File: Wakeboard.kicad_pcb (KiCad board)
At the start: 2 copper layers, 30.6 x 58.6 mm, 34 parts, among them CN1 JST S2B-PH-SM4-TB(LF)(SN), J2 HCTL HC-TYPE-C-16P-01A, Q1 DMP2045UQ-7, SW1 TS-1088-AR02016, SW2 TS-1088-AR02016, U1 RT9080-33GJ5, U2 ESP32-S3-MINI-1, U3 LIS3DHTR_C15134, U4 MCP73831T-2ACI/OT

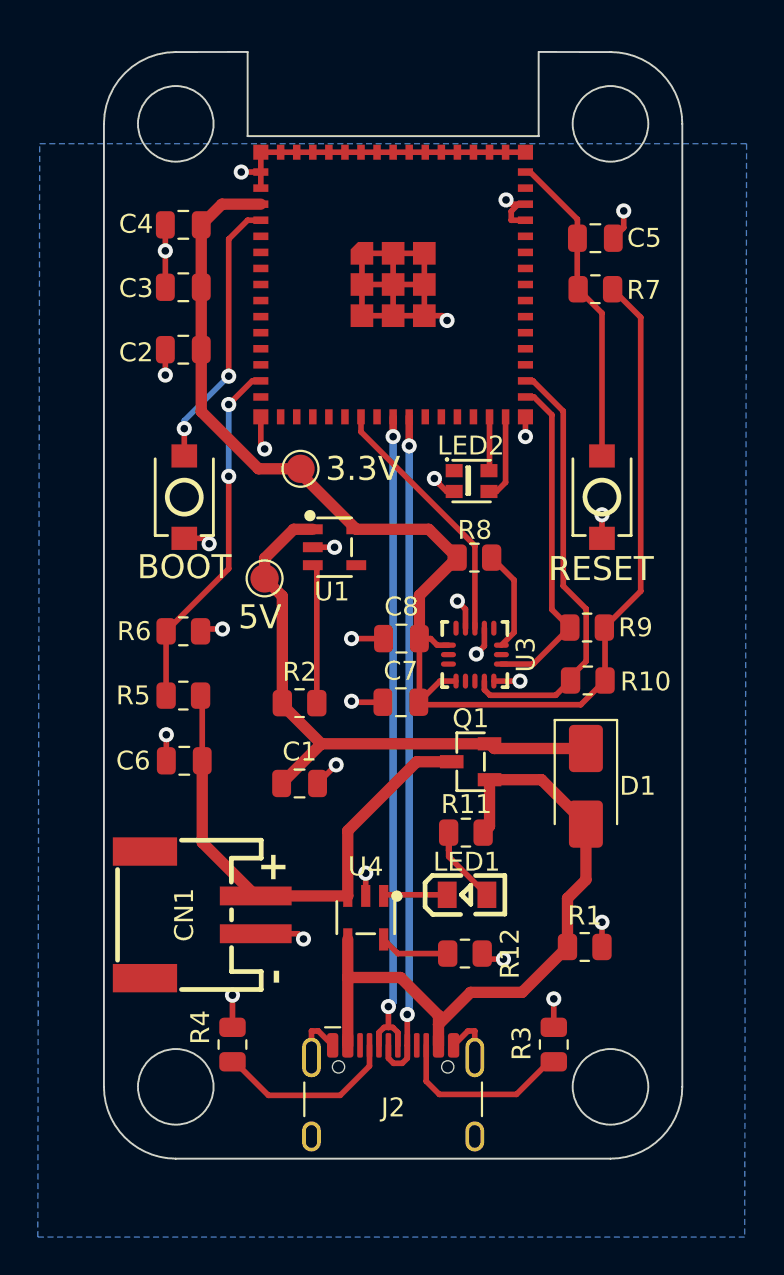
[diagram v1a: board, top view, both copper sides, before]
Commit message: Shift battery socket
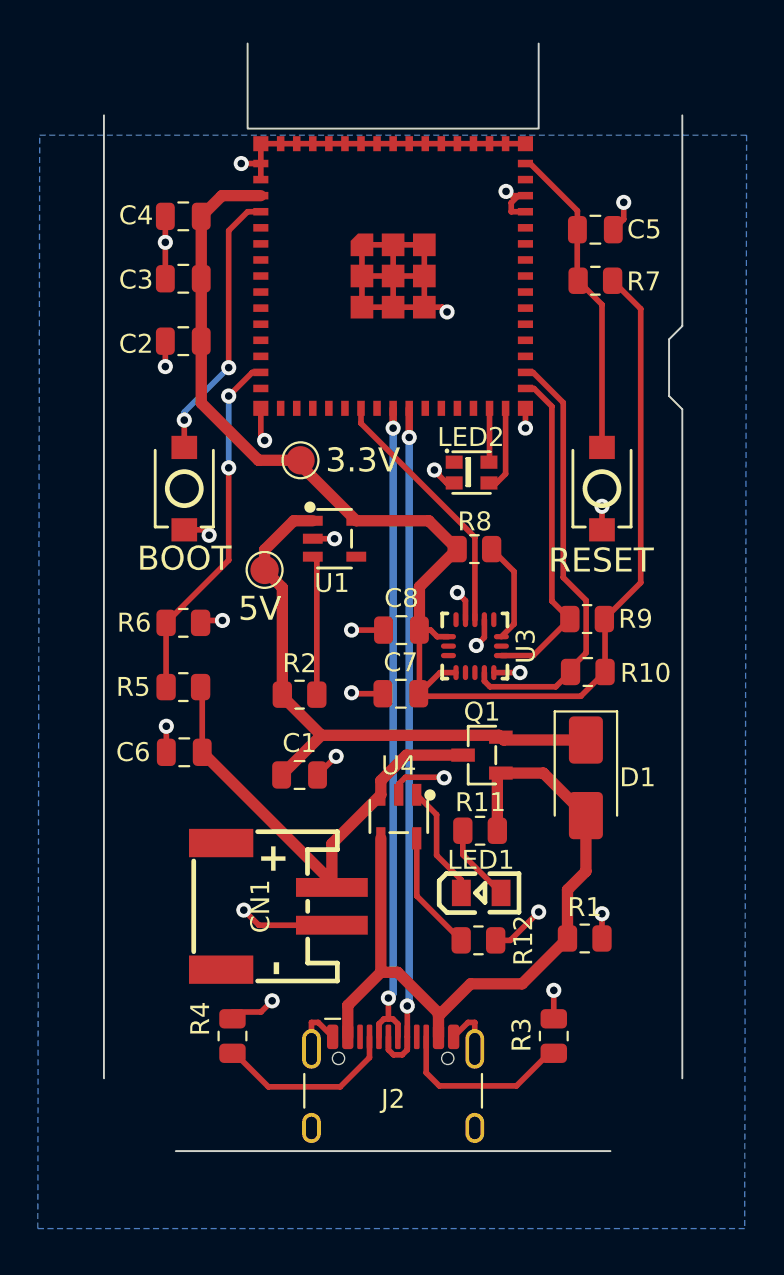
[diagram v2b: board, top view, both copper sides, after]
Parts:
- moved U4 5.63 mm to (127.8, 84.9)
- moved CN1 4.06 mm to (121.3, 89.7)
- moved R12 1.00 mm to (132.0, 91.5)
- moved LED1 0.76 mm to (132.2, 88.9)
- moved R11 0.76 mm to (132.1, 85.7)
- moved Q1 0.69 mm to (132.2, 81.7)
- moved C1 0.45 mm to (122.5, 82.7)
- moved C2 0.45 mm to (116.4, 59.7)
- moved C3 0.45 mm to (116.4, 56.4)
- moved C4 0.45 mm to (116.4, 53.1)
- moved C6 0.45 mm to (116.5, 81.5)
- moved C7 0.45 mm to (127.9, 78.4)
- moved C8 0.45 mm to (127.9, 75.0)
- moved D1 0.45 mm to (137.7, 82.8)
- moved J2 0.45 mm to (127.5, 100.3)
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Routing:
- net GND: track 82.0 -> 88.9 mm
- net VBUS: track 37.3 -> 40.4 mm
- net Net-(LED1--): track 3.38 -> 6.17 mm
- net Net-(U4-PROG): track 3.70 -> 6.37 mm
- net VBAT: track 27.1 -> 25.1 mm
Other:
- outline, holes or cut-outs redrawn

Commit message: Remove mounting holes. Fix minor things
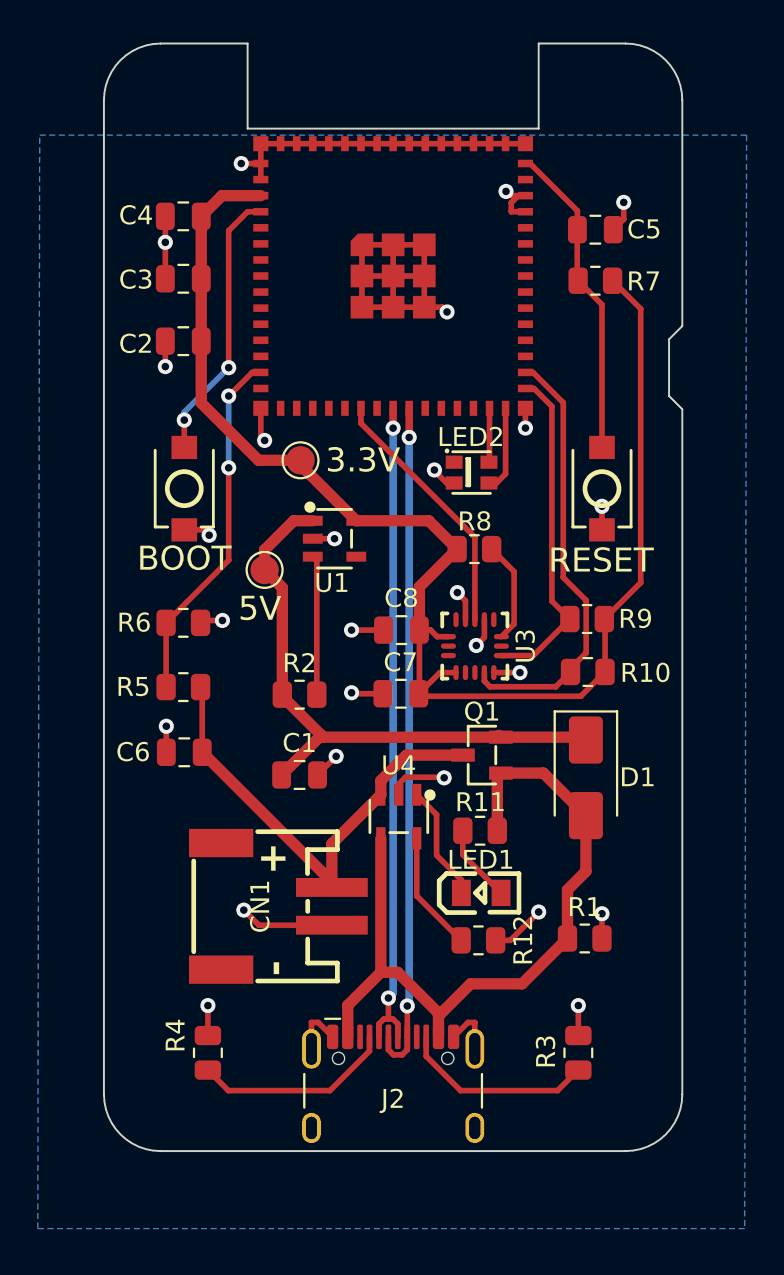
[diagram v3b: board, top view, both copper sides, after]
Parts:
- moved R3 1.57 mm to (137.3, 97.4)
- moved R4 1.57 mm to (117.7, 97.4)
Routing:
- net Net-(J2-CC1): track 9.77 -> 10.6 mm
- net Net-(J2-CC2): track 9.58 -> 10.3 mm
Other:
- outline, holes or cut-outs redrawn
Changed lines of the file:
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@@
 	(footprint "Resistor_SMD:R_0805_2012Metric"
 		(layer "F.Cu")
-		(at 136 96.5125 -90)
+		(at 137.3 97.4 -90)
 		(descr "Resistor SMD 0805 (2012 Metric), square (rectangular) end terminal, IPC_7351 nominal, (Body size source: IPC-SM-782 page 72, https://www.pcb-3d.com/wordpress/wp-content/uploads/ipc-sm-782a_amendment_1_and_2.pdf), generated with kicad-footprint-generator")
 		(tags "resistor")
@@
 	(footprint "Resistor_SMD:R_0805_2012Metric"
 		(layer "F.Cu")
-		(at 119 96.5125 -90)
+		(at 117.7 97.4 -90)
 		(descr "Resistor SMD 0805 (2012 Metric), square (rectangular) end terminal, IPC_7351 nominal, (Body size source: IPC-SM-782 page 72, https://www.pcb-3d.com/wordpress/wp-content/uploads/ipc-sm-782a_amendment_1_and_2.pdf), generated with kicad-footprint-generator")
 		(tags "resistor")
@@
 		(layer "B.SilkS")
 	)
+	(gr_arc
+		(start 142.8 99.6)
+		(mid 141.92132 101.72132)
+		(end 139.8 102.6)
+		(stroke
+			(width 0.1)
+			(type default)
+		)
+		(layer "Edge.Cuts")
+	)
 	(gr_line
 		(start 142.1 59.65)
@@
 	)
 	(gr_line
-		(start 142.799658 47.803044)
+		(start 142.8 47)
 		(end 142.8 58.95)
 		(stroke
@@
 	(gr_line
 		(start 142.8 63.35)
-		(end 142.8 98.75)
+		(end 142.8 99.6)
 		(stroke
 			(width 0.1)
@@
 	)
 	(gr_line
-		(start 119.8 48.45)
+		(start 119.8 48.5)
 		(end 119.8 44)
 		(stroke
@@
 		(layer "Edge.Cuts")
 	)
+	(gr_arc
+		(start 115.2 102.6)
+		(mid 113.07868 101.72132)
+		(end 112.2 99.6)
+		(stroke
+			(width 0.1)
+			(type default)
+		)
+		(layer "Edge.Cuts")
+	)
+	(gr_arc
+		(start 139.8 44)
+		(mid 141.92132 44.87868)
+		(end 142.8 47)
+		(stroke
+			(width 0.1)
+			(type default)
+		)
+		(layer "Edge.Cuts")
+	)
 	(gr_line
-		(start 112.199829 47.797938)
-		(end 112.2 98.75)
+		(start 112.2 47)
+		(end 112.2 99.6)
 		(stroke
 			(width 0.1)
@@
 	)
 	(gr_line
-		(start 116 102.6)
-		(end 139 102.6)
+		(start 115.2 102.6)
+		(end 139.8 102.6)
 		(stroke
 			(width 0.1)
@@
 	(gr_line
 		(start 135.2 44)
-		(end 135.2 48.45)
+		(end 139.8 44)
+		(stroke
+			(width 0.1)
+			(type default)
+		)
+		(layer "Edge.Cuts")
+	)
+	(gr_line
+		(start 119.8 44)
+		(end 115.2 44)
+		(stroke
+			(width 0.1)
+			(type default)
+		)
+		(layer "Edge.Cuts")
+	)
+	(gr_line
+		(start 135.2 44)
+		(end 135.2 48.5)
 		(stroke
 			(width 0.1)
@@
 		(layer "Edge.Cuts")
 	)
+	(gr_arc
+		(start 112.2 47)
+		(mid 113.07868 44.87868)
+		(end 115.2 44)
+		(stroke
+			(width 0.1)
+			(type default)
+		)
+		(layer "Edge.Cuts")
+	)
 	(gr_text "-"
 		(at 122.1 93.35 90)
@@
 	)
 	(segment
-		(start 133.35 80.85)
-		(end 133.2 80.7)
+		(start 120.7 71.85)
+		(end 120.7 70.78934)
 		(width 0.6)
 		(layer "F.Cu")
@@
 	)
 	(segment
-		(start 120.7 71.85)
-		(end 120.7 70.78934)
+		(start 133.2 80.7)
+		(end 133.1 80.6)
 		(width 0.6)
 		(layer "F.Cu")
@@
 	)
 	(segment
-		(start 133.2 80.7)
-		(end 133.1 80.6)
+		(start 137.55 80.7)
+		(end 137.7 80.85)
 		(width 0.6)
 		(layer "F.Cu")
@@
 	)
 	(segment
-		(start 122.23934 69.25)
-		(end 123.25 69.25)
+		(start 133.2 80.7)
+		(end 123.8 80.7)
 		(width 0.6)
 		(layer "F.Cu")
@@
 	)
 	(segment
-		(start 133.1 80.6)
-		(end 123.7 80.6)
+		(start 122.23934 69.25)
+		(end 123.25 69.25)
 		(width 0.6)
 		(layer "F.Cu")
@@
 	)
 	(segment
+		(start 123.8 80.7)
+		(end 123.7 80.6)
+		(width 0.6)
+		(layer "F.Cu")
+		(net 31)
+	)
+	(segment
+		(start 133.2 80.7)
+		(end 137.55 80.7)
+		(width 0.6)
+		(layer "F.Cu")
+		(net 31)
+	)
+	(segment
 		(start 121.6375 78.45)
 		(end 121.6375 78.5375)
@@
 	)
 	(segment
-		(start 137.7 80.85)
-		(end 133.35 80.85)
-		(width 0.6)
-		(layer "F.Cu")
-		(net 31)
-	)
-	(segment
 		(start 121.6375 78.45)
 		(end 121.6375 72.7875)
@@
 	)
 	(segment
-		(start 121.1 94.65)
-		(end 120.5094 95.2406)
+		(start 117.7 96.4875)
+		(end 117.7 94.9)
 		(width 0.3)
 		(layer "F.Cu")
@@
 	)
 	(segment
-		(start 120.5094 95.2406)
-		(end 119 95.2406)
-		(width 0.3)
-		(layer "F.Cu")
-		(net 32)
-	)
-	(segment
 		(start 134.5 52.9)
 		(end 133.7483 52.9)
@@
 	)
 	(segment
+		(start 137.3 96.4875)
+		(end 137.3 94.9)
+		(width 0.3)
+		(layer "F.Cu")
+		(net 32)
+	)
+	(segment
 		(start 127.5 56.3)
 		(end 127.5 57.95)
@@
 	)
 	(segment
-		(start 136 94.09475)
-		(end 136 95.40525)
-		(width 0.3)
-		(layer "F.Cu")
-		(net 32)
-	)
-	(segment
 		(start 128.35 49.3)
 		(end 127.5 49.3)
@@
 	)
 	(via
-		(at 138.55 68.4835)
+		(at 117.7 94.9)
 		(size 0.8)
 		(drill 0.4)
@@
 	)
 	(via
-		(at 115.5 80.1225)
+		(at 138.55 68.4835)
 		(size 0.8)
 		(drill 0.4)
@@
 	)
 	(via
-		(at 124.4 70.2)
+		(at 115.5 80.1225)
 		(size 0.8)
 		(drill 0.4)
@@
 	)
 	(via
-		(at 134.210794 77.282498)
+		(at 124.4 70.2)
 		(size 0.8)
 		(drill 0.4)
@@
 	)
 	(via
-		(at 134.5 64.3465)
+		(at 134.210794 77.282498)
 		(size 0.8)
 		(drill 0.4)
@@
 	)
 	(via
-		(at 135.2 89.95)
+		(at 134.5 64.3465)
 		(size 0.8)
 		(drill 0.4)
@@
 	)
 	(via
-		(at 121.1 94.65)
+		(at 135.2 89.95)
 		(size 0.8)
 		(drill 0.4)
@@
 	)
 	(via
-		(at 136 94.09475)
+		(at 130.2 82.85)
 		(size 0.8)
 		(drill 0.4)
@@
 	)
 	(via
-		(at 130.2 82.85)
+		(at 139.7 52.4056)
 		(size 0.8)
 		(drill 0.4)
@@
 	)
 	(via
-		(at 139.7 52.4056)
+		(at 129.683228 66.562164)
 		(size 0.8)
 		(drill 0.4)
@@
 	)
 	(via
-		(at 129.683228 66.562164)
+		(at 115.448 54.5198)
 		(size 0.8)
 		(drill 0.4)
@@
 	)
 	(via
-		(at 115.448 54.5198)
+		(at 137.3 94.9)
 		(size 0.8)
 		(drill 0.4)
@@
 	)
 	(segment
-		(start 134.025 99.15)
-		(end 129.945 99.15)
+		(start 137.0175 98.595)
+		(end 137.005 98.595)
+		(width 0.3)
+		(layer "F.Cu")
+		(net 38)
+	)
+	(segment
+		(start 137.3 98.3125)
+		(end 137.0175 98.595)
 		(width 0.3)
 		(layer "F.Cu")
@@
 	)
 	(segment
-		(start 129.25 98.455)
+		(start 129.25 97.580305)
 		(end 129.25 96.555)
 		(width 0.3)
@@
 	)
 	(segment
-		(start 135.875 97.3)
-		(end 134.025 99.15)
+		(start 131.069695 99.4)
+		(end 129.25 97.580305)
 		(width 0.3)
 		(layer "F.Cu")
@@
 	)
 	(segment
-		(start 129.945 99.15)
-		(end 129.25 98.455)
+		(start 136.2 99.4)
+		(end 131.069695 99.4)
 		(width 0.3)
 		(layer "F.Cu")
@@
 	)
 	(segment
-		(start 120.9 99.2)
-		(end 124.7 99.2)
+		(start 137.005 98.595)
+		(end 136.2 99.4)
+		(width 0.3)
+		(layer "F.Cu")
+		(net 38)
+	)
+	(segment
+		(start 126.25 97.30812)
+		(end 126.25 96.555)
 		(width 0.3)
 		(layer "F.Cu")
@@
 	)
 	(segment
-		(start 119 97.3)
-		(end 120.9 99.2)
+		(start 117.7 98.3125)
+		(end 118.7875 99.4)
 		(width 0.3)
 		(layer "F.Cu")
@@
 	)
 	(segment
-		(start 124.7 99.2)
-		(end 126.25 97.65)
+		(start 124.15812 99.4)
+		(end 126.25 97.30812)
 		(width 0.3)
 		(layer "F.Cu")
@@
 	)
 	(segment
-		(start 126.25 97.65)
-		(end 126.25 96.555)
+		(start 118.7875 99.4)
+		(end 124.15812 99.4)
 		(width 0.3)
 		(layer "F.Cu")

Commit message: Enclosure OpenSCAD files
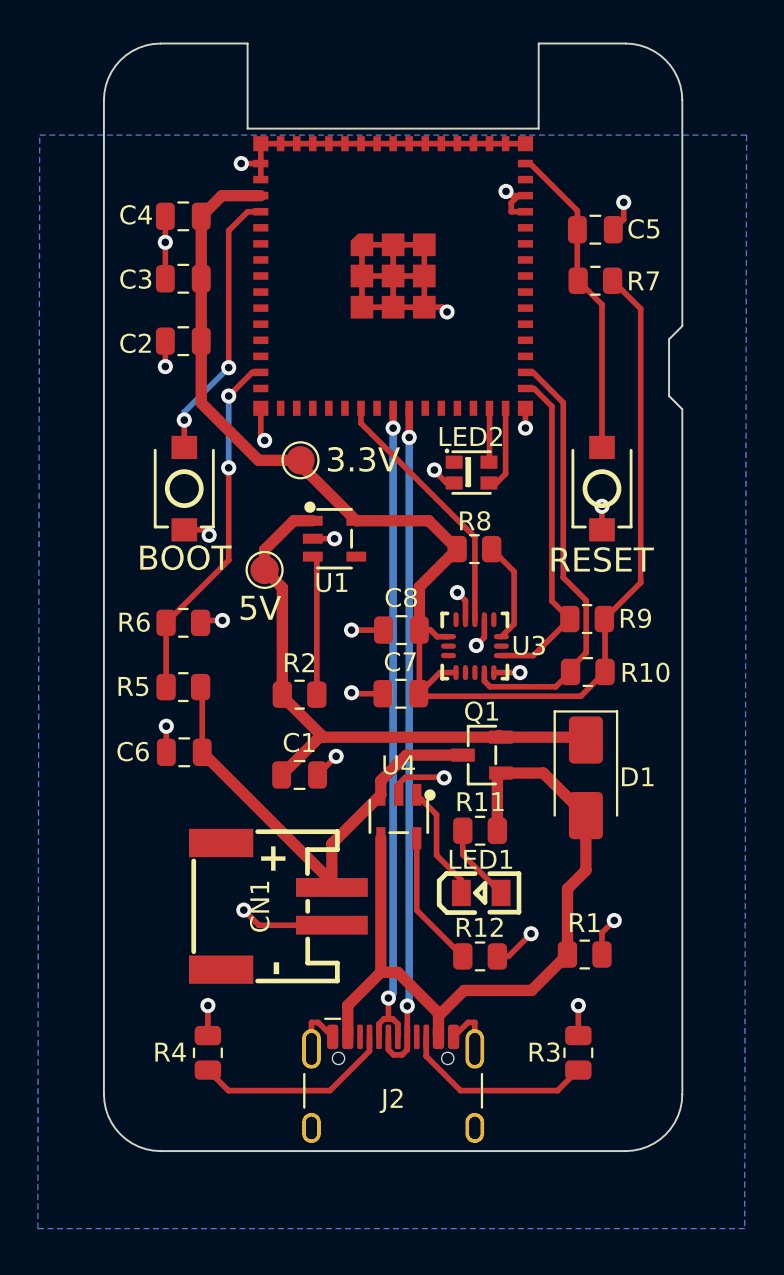
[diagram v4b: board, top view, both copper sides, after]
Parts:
- moved R12 0.85 mm to (132.1, 92.3)
- moved R1 0.85 mm to (137.6, 92.2)
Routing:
- net Net-(U4-PROG): track 6.37 -> 7.26 mm
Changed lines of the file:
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@@
 		(tags "resistor")
 		(property "Reference" "R3"
-			(at -0.0625 1.7 90)
+			(at 0 1.8 180)
 			(layer "F.SilkS")
 			(effects
@@
 		)
 		(property "Value" "5.1K"
-			(at 0.0375 -0.1 90)
+			(at 0 -1.8 90)
 			(layer "F.Fab")
 			(effects
@@
 	(footprint "Resistor_SMD:R_0805_2012Metric"
 		(layer "F.Cu")
-		(at 132.0125 91.45)
+		(at 132.1 92.3)
 		(descr "Resistor SMD 0805 (2012 Metric), square (rectangular) end terminal, IPC_7351 nominal, (Body size source: IPC-SM-782 page 72, https://www.pcb-3d.com/wordpress/wp-content/uploads/ipc-sm-782a_amendment_1_and_2.pdf), generated with kicad-footprint-generator")
 		(tags "resistor")
 		(property "Reference" "R12"
-			(at 2.380301 0.000448 -90)
+			(at -0.0125 -1.5 0)
 			(layer "F.SilkS")
 			(effects
@@
 		)
 		(property "Value" "2k"
-			(at 0 1.65 0)
+			(at 0 1.5 0)
 			(layer "F.Fab")
 			(effects
@@
 		(tags "resistor")
 		(property "Reference" "R4"
-			(at -0.9125 1.7 90)
+			(at -0.000001 1.999999 180)
 			(layer "F.SilkS")
 			(effects
@@
 		)
 		(property "Value" "5.1K"
-			(at 0 -1.6 90)
+			(at 0 -1.7 90)
 			(layer "F.Fab")
 			(effects
@@
 		(at 131.8275 75.882498 90)
 		(property "Reference" "U3"
-			(at 0.000274 2.693298 -90)
+			(at 0.000274 2.8725 0)
 			(layer "F.SilkS")
 			(effects
@@
 	(footprint "Resistor_SMD:R_0805_2012Metric"
 		(layer "F.Cu")
-		(at 137.6375 91.35)
+		(at 137.6375 92.2)
 		(descr "Resistor SMD 0805 (2012 Metric), square (rectangular) end terminal, IPC_7351 nominal, (Body size source: IPC-SM-782 page 72, https://www.pcb-3d.com/wordpress/wp-content/uploads/ipc-sm-782a_amendment_1_and_2.pdf), generated with kicad-footprint-generator")
 		(tags "resistor")
@@
 	)
 	(segment
-		(start 138.55 90.0414)
-		(end 138.55 91.35)
-		(width 0.3)
-		(layer "F.Cu")
-		(net 32)
-	)
-	(segment
 		(start 131.3275 73.4775)
 		(end 130.9 73.05)
@@
 	)
 	(segment
-		(start 132.925 91.45)
-		(end 133.7 91.45)
+		(start 134.1242 52.05)
+		(end 133.7483 52.05)
 		(width 0.3)
 		(layer "F.Cu")
@@
 	)
 	(segment
-		(start 134.1242 52.05)
-		(end 133.7483 52.05)
+		(start 138.55 92.2)
+		(end 138.55 91.05)
 		(width 0.3)
 		(layer "F.Cu")
@@
 	)
 	(segment
-		(start 133.7 91.45)
-		(end 135.2 89.95)
-		(width 0.3)
-		(layer "F.Cu")
-		(net 32)
-	)
-	(segment
 		(start 129.15 56.3)
 		(end 129.15 54.65)
@@
 	)
 	(segment
+		(start 138.55 91.05)
+		(end 139.2 90.4)
+		(width 0.3)
+		(layer "F.Cu")
+		(net 32)
+	)
+	(segment
+		(start 133.0125 92.3)
+		(end 133.6 92.3)
+		(width 0.3)
+		(layer "F.Cu")
+		(net 32)
+	)
+	(segment
 		(start 127.5 49.3)
 		(end 126.65 49.3)
@@
 	)
 	(segment
+		(start 133.6 92.3)
+		(end 134.8 91.1)
+		(width 0.3)
+		(layer "F.Cu")
+		(net 32)
+	)
+	(segment
 		(start 138.55 69.73)
 		(end 138.55 68.4835)
@@
 	)
 	(via
-		(at 138.55 90.0414)
+		(at 139.2 90.4)
 		(size 0.8)
 		(drill 0.4)
@@
 	)
 	(via
-		(at 135.2 89.95)
+		(at 130.2 82.85)
 		(size 0.8)
 		(drill 0.4)
@@
 	)
 	(via
-		(at 130.2 82.85)
+		(at 134.8 91.1)
 		(size 0.8)
 		(drill 0.4)
@@
 	)
 	(segment
-		(start 134.325 93.75)
-		(end 131.6 93.75)
+		(start 137.7 87.747493)
+		(end 136.725 88.722493)
 		(width 0.6)
 		(layer "F.Cu")
@@
 	)
 	(segment
-		(start 137.7 87.8)
-		(end 137.7 84.85)
+		(start 136.725 92.2)
+		(end 134.825 94.1)
 		(width 0.6)
 		(layer "F.Cu")
@@
 	)
 	(segment
-		(start 133.0125 82.7875)
-		(end 133.2 82.6)
+		(start 137.7 84.85)
+		(end 137.7 87.747493)
 		(width 0.6)
 		(layer "F.Cu")
@@
 	)
 	(segment
-		(start 136.725 91.35)
-		(end 136.725 88.775)
+		(start 133.0125 82.7875)
+		(end 133.2 82.6)
 		(width 0.6)
 		(layer "F.Cu")
@@
 	)
 	(segment
-		(start 136.725 88.775)
-		(end 137.7 87.8)
+		(start 131.25 94.1)
+		(end 129.9 95.45)
 		(width 0.6)
 		(layer "F.Cu")
@@
 	)
 	(segment
-		(start 133.0125 85.65)
-		(end 133.0125 82.7875)
+		(start 136.725 88.722493)
+		(end 136.725 92.2)
 		(width 0.6)
 		(layer "F.Cu")
@@
 	)
 	(segment
-		(start 131.6 93.75)
-		(end 129.9 95.45)
+		(start 134.825 94.1)
+		(end 131.25 94.1)
 		(width 0.6)
 		(layer "F.Cu")
@@
 	)
 	(segment
-		(start 136.725 91.35)
-		(end 134.325 93.75)
+		(start 133.0125 85.65)
+		(end 133.0125 82.7875)
 		(width 0.6)
 		(layer "F.Cu")
@@
 	)
 	(segment
-		(start 128.75 86.05)
-		(end 128.75 89.1)
+		(start 131.1875 92.3)
+		(end 128.75 89.8625)
 		(width 0.3)
 		(layer "F.Cu")
@@
 	)
 	(segment
-		(start 128.75 89.1)
-		(end 131.1 91.45)
+		(start 128.75 89.8625)
+		(end 128.75 86.05)
 		(width 0.3)
 		(layer "F.Cu")
